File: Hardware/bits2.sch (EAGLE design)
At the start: 25 parts, among them X1 22-23-2021, X2 53398-10, X3 22-23-2031, X4 22-23-2041

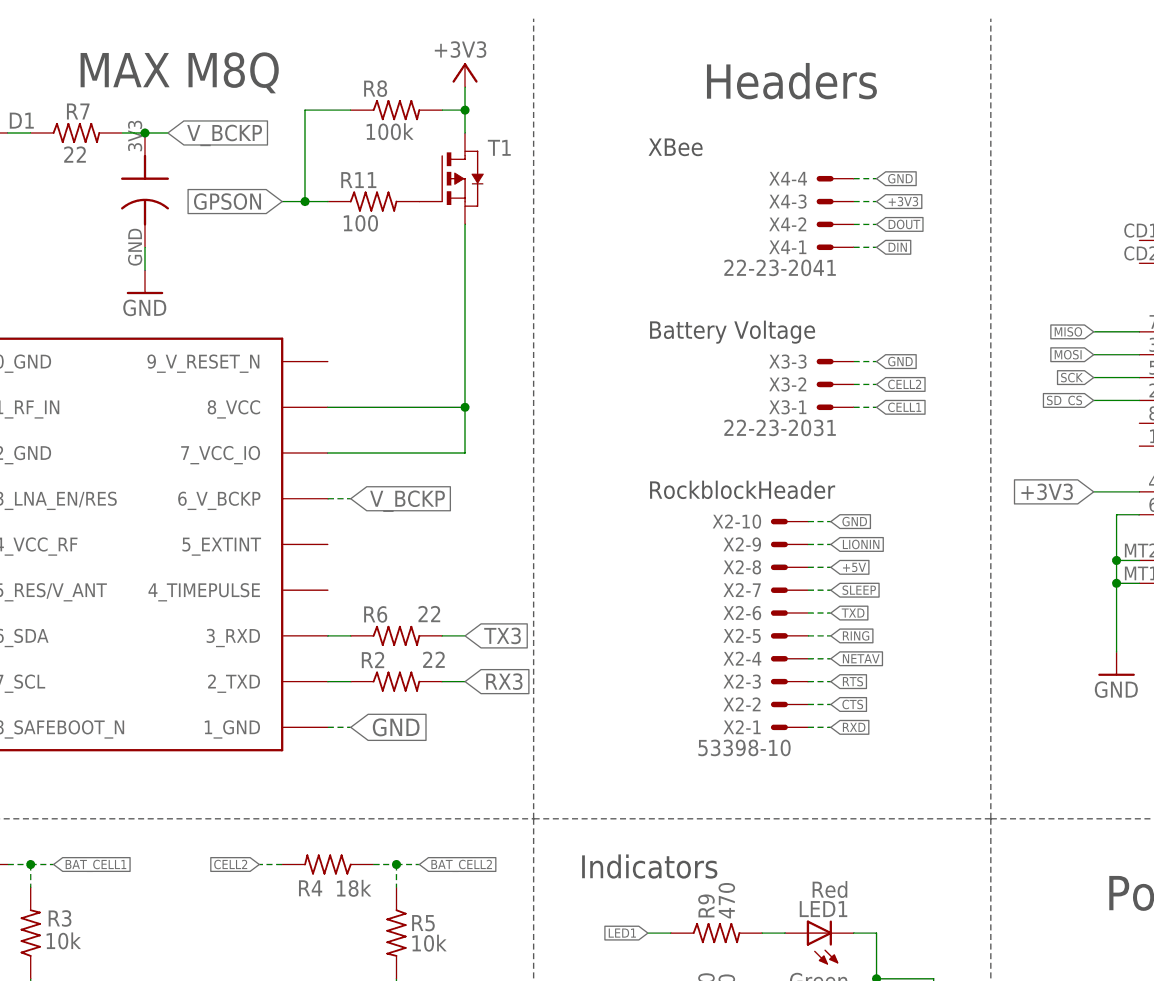
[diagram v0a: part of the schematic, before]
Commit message: Flipped the GPS mosfet around
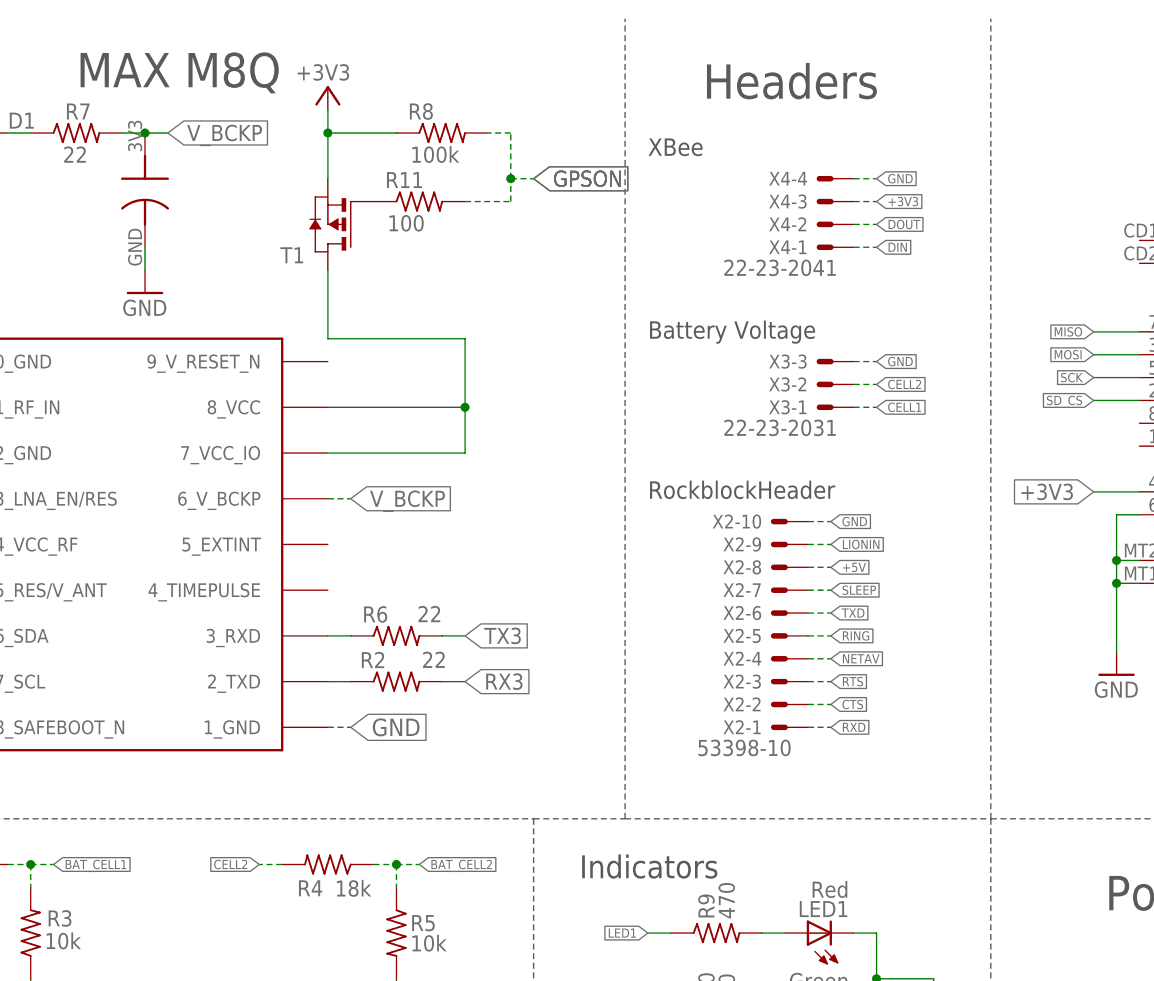
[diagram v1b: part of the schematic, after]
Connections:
- removed net N$7: R11.2, T1.G
- new net N$9: R11.1, T1.G
- net +3V3: now also R8.1, T1.S; no longer R8.2, T1.D
- net GPSON: now also R11.2, R8.2; no longer R11.1, R8.1
- net N$11: now also T1.D; no longer T1.S
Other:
- moved on the sheet: R11, R8, T1
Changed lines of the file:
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@@
 <?xml version="1.0" encoding="utf-8"?>
 <!DOCTYPE eagle SYSTEM "eagle.dtd">
-<eagle version="9.3.0">
+<eagle version="9.2.2">
 <drawing>
 <settings>
-<setting alwaysvectorfont="no"/>
+<setting alwaysvectorfont="yes"/>
 <setting verticaltext="up"/>
 </settings>
@@
 <wire x1="86.36" y1="38.1" x2="86.36" y2="7.62" width="0.1524" layer="97" style="longdash"/>
 <wire x1="86.36" y1="38.1" x2="167.64" y2="38.1" width="0.1524" layer="97" style="longdash"/>
-<wire x1="167.64" y1="38.1" x2="167.64" y2="127" width="0.1524" layer="97" style="longdash"/>
 <wire x1="167.64" y1="38.1" x2="167.64" y2="7.62" width="0.1524" layer="97" style="longdash"/>
-<wire x1="167.64" y1="38.1" x2="218.44" y2="38.1" width="0.1524" layer="97" style="longdash"/>
+<wire x1="167.64" y1="38.1" x2="177.8" y2="38.1" width="0.1524" layer="97" style="longdash"/>
+<wire x1="177.8" y1="38.1" x2="218.44" y2="38.1" width="0.1524" layer="97" style="longdash"/>
 <wire x1="218.44" y1="38.1" x2="266.7" y2="38.1" width="0.1524" layer="97" style="longdash"/>
 <wire x1="218.44" y1="38.1" x2="218.44" y2="127" width="0.1524" layer="97" style="longdash"/>
@@
 <text x="180.34" y="91.44" size="1.9304" layer="97">Battery Voltage</text>
 <text x="180.34" y="111.76" size="1.9304" layer="97">XBee</text>
+<wire x1="177.8" y1="38.1" x2="177.8" y2="127" width="0.1524" layer="97" style="longdash"/>
 </plain>
 <instances>
@@
 <attribute name="VALUE" x="99.06" y="119.38" size="1.778" layer="96" rot="R90"/>
 </instance>
-<instance part="T1" gate="A" x="160.02" y="109.22" smashed="yes">
-<attribute name="VALUE" x="162.56" y="109.22" size="1.778" layer="96"/>
-<attribute name="NAME" x="162.56" y="111.76" size="1.778" layer="95"/>
-</instance>
-<instance part="R8" gate="G$1" x="152.4" y="116.84" smashed="yes">
-<attribute name="NAME" x="148.59" y="118.3386" size="1.778" layer="95"/>
-<attribute name="VALUE" x="148.844" y="113.538" size="1.778" layer="96"/>
-</instance>
-<instance part="+3V2" gate="G$1" x="160.02" y="121.92" smashed="yes">
-<attribute name="VALUE" x="162.56" y="124.46" size="1.778" layer="96" rot="R180"/>
-</instance>
-<instance part="R11" gate="G$1" x="149.86" y="106.68" smashed="yes">
-<attribute name="NAME" x="146.05" y="108.1786" size="1.778" layer="95"/>
-<attribute name="VALUE" x="146.304" y="103.378" size="1.778" layer="96"/>
+<instance part="T1" gate="A" x="144.78" y="104.14" smashed="yes" rot="R180">
+<attribute name="VALUE" x="142.24" y="104.14" size="1.778" layer="96" rot="R180"/>
+<attribute name="NAME" x="142.24" y="101.6" size="1.778" layer="95" rot="R180"/>
+</instance>
+<instance part="R8" gate="G$1" x="157.48" y="114.3" smashed="yes">
+<attribute name="NAME" x="153.67" y="115.7986" size="1.778" layer="95"/>
+<attribute name="VALUE" x="153.924" y="110.998" size="1.778" layer="96"/>
+</instance>
+<instance part="+3V2" gate="G$1" x="144.78" y="119.38" smashed="yes">
+<attribute name="VALUE" x="147.32" y="121.92" size="1.778" layer="96" rot="R180"/>
+</instance>
+<instance part="R11" gate="G$1" x="154.94" y="106.68" smashed="yes">
+<attribute name="NAME" x="151.13" y="108.1786" size="1.778" layer="95"/>
+<attribute name="VALUE" x="151.384" y="103.378" size="1.778" layer="96"/>
 </instance>
 </instances>
@@
 </segment>
 <segment>
-<pinref part="R8" gate="G$1" pin="2"/>
-<pinref part="T1" gate="A" pin="D"/>
-<wire x1="157.48" y1="116.84" x2="160.02" y2="116.84" width="0.1524" layer="91"/>
-<wire x1="160.02" y1="116.84" x2="160.02" y2="114.3" width="0.1524" layer="91"/>
-<wire x1="160.02" y1="116.84" x2="160.02" y2="119.38" width="0.1524" layer="91"/>
-<junction x="160.02" y="116.84"/>
 <pinref part="+3V2" gate="G$1" pin="+3V3"/>
+<pinref part="T1" gate="A" pin="S"/>
+<wire x1="144.78" y1="116.84" x2="144.78" y2="114.3" width="0.1524" layer="91"/>
+<pinref part="R8" gate="G$1" pin="1"/>
+<wire x1="144.78" y1="114.3" x2="144.78" y2="109.22" width="0.1524" layer="91"/>
+<wire x1="152.4" y1="114.3" x2="144.78" y2="114.3" width="0.1524" layer="91"/>
+<junction x="144.78" y="114.3"/>
 </segment>
 </net>
@@
 </segment>
 <segment>
-<wire x1="144.78" y1="106.68" x2="142.24" y2="106.68" width="0.1524" layer="91"/>
-<label x="139.7" y="106.68" size="1.778" layer="95" rot="R180" xref="yes"/>
-<pinref part="R11" gate="G$1" pin="1"/>
-<pinref part="R8" gate="G$1" pin="1"/>
-<wire x1="142.24" y1="106.68" x2="139.7" y2="106.68" width="0.1524" layer="91"/>
-<wire x1="147.32" y1="116.84" x2="142.24" y2="116.84" width="0.1524" layer="91"/>
-<wire x1="142.24" y1="116.84" x2="142.24" y2="106.68" width="0.1524" layer="91"/>
-<junction x="142.24" y="106.68"/>
+<pinref part="R11" gate="G$1" pin="2"/>
+<wire x1="160.02" y1="106.68" x2="165.1" y2="106.68" width="0.1524" layer="91" style="longdash"/>
+<wire x1="165.1" y1="106.68" x2="165.1" y2="109.22" width="0.1524" layer="91" style="longdash"/>
+<pinref part="R8" gate="G$1" pin="2"/>
+<wire x1="165.1" y1="109.22" x2="165.1" y2="114.3" width="0.1524" layer="91" style="longdash"/>
+<wire x1="165.1" y1="114.3" x2="162.56" y2="114.3" width="0.1524" layer="91" style="longdash"/>
+<wire x1="165.1" y1="109.22" x2="167.64" y2="109.22" width="0.1524" layer="91" style="longdash"/>
+<junction x="165.1" y="109.22"/>
+<label x="167.64" y="109.22" size="1.778" layer="95" xref="yes"/>
+<label x="167.64" y="109.22" size="1.778" layer="95" xref="yes"/>
 </segment>
 </net>
@@
 <net name="N$11" class="0">
 <segment>
-<pinref part="T1" gate="A" pin="S"/>
 <wire x1="160.02" y1="78.74" x2="160.02" y2="83.82" width="0.1524" layer="91"/>
 <pinref part="U$7" gate="G$1" pin="7_VCC_IO"/>
-<wire x1="160.02" y1="83.82" x2="160.02" y2="104.14" width="0.1524" layer="91"/>
 <wire x1="144.78" y1="78.74" x2="160.02" y2="78.74" width="0.1524" layer="91"/>
 <pinref part="U$7" gate="G$1" pin="8_VCC"/>
 <wire x1="144.78" y1="83.82" x2="160.02" y2="83.82" width="0.1524" layer="91"/>
+<pinref part="T1" gate="A" pin="D"/>
+<wire x1="144.78" y1="99.06" x2="144.78" y2="91.44" width="0.1524" layer="91"/>
+<wire x1="144.78" y1="91.44" x2="160.02" y2="91.44" width="0.1524" layer="91"/>
+<wire x1="160.02" y1="91.44" x2="160.02" y2="83.82" width="0.1524" layer="91"/>
 <junction x="160.02" y="83.82"/>
 </segment>
@@
 </segment>
 </net>
-<net name="N$7" class="0">
-<segment>
+<net name="N$9" class="0">
+<segment>
+<pinref part="R11" gate="G$1" pin="1"/>
 <pinref part="T1" gate="A" pin="G"/>
-<pinref part="R11" gate="G$1" pin="2"/>
-</segment>
-</net>
+</segment>
+</net>

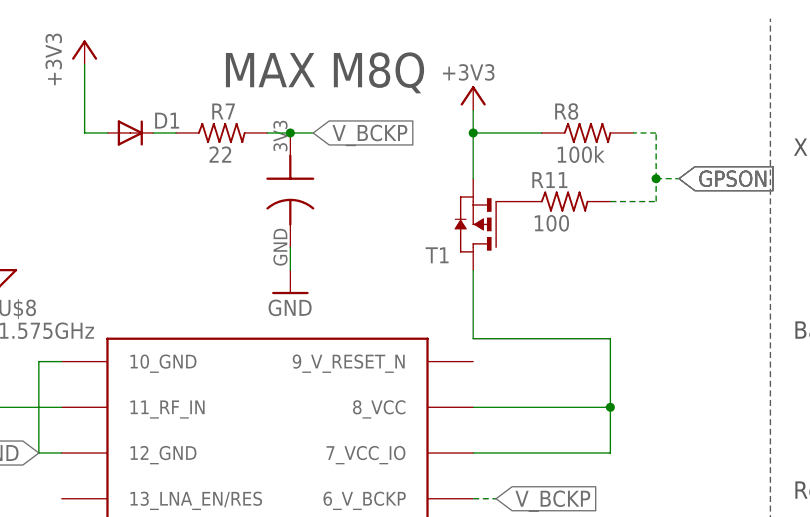
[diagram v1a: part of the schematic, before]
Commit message: Added value for gps Mosfet
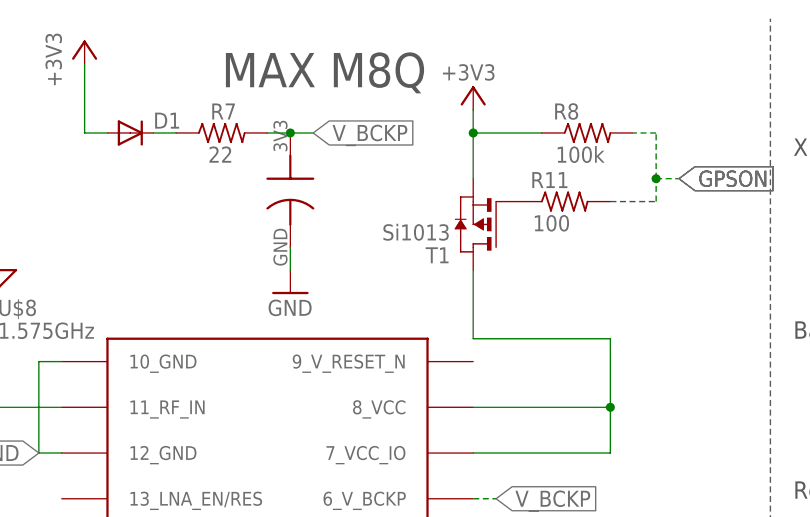
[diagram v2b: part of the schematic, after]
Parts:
- T1: value (none) -> Si1013; SPICEPREFIX (none) -> J
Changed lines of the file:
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@@
 <part name="D1" library="diode" library_urn="urn:adsk.eagle:library:210" deviceset="DIODE-" device="SOD523" package3d_urn="urn:adsk.eagle:package:43410/1"/>
 <part name="+3V1" library="supply1" library_urn="urn:adsk.eagle:library:371" deviceset="+3V3" device=""/>
-<part name="T1" library="zetex" library_urn="urn:adsk.eagle:library:418" deviceset="PMOSSOT23" device="" package3d_urn="urn:adsk.eagle:package:30981/1"/>
+<part name="T1" library="zetex" library_urn="urn:adsk.eagle:library:418" deviceset="PMOSSOT23" device="" package3d_urn="urn:adsk.eagle:package:30981/1" value="Si1013">
+<attribute name="SPICEPREFIX" value="J"/>
+</part>
 <part name="R8" library="rcl" library_urn="urn:adsk.eagle:library:334" deviceset="R-US_" device="R0603" package3d_urn="urn:adsk.eagle:package:23555/2" value="100k"/>
 <part name="+3V2" library="supply1" library_urn="urn:adsk.eagle:library:371" deviceset="+3V3" device=""/>
